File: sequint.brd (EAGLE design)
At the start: 70 x 80 mm, 72 parts, among them IC1 STM32F10XCXT6, Q1 MOSFET-NCHANNELSMD, Q2 MOSFET-NCHANNELSMD, Q3 MOSFET-NCHANNELSMD, Q4 MOSFET-NCHANNELSMD, Q5 16MHz, U1 LSM330DLCTRLGA, U2 MCP73831, U4 NRF24L01SMD

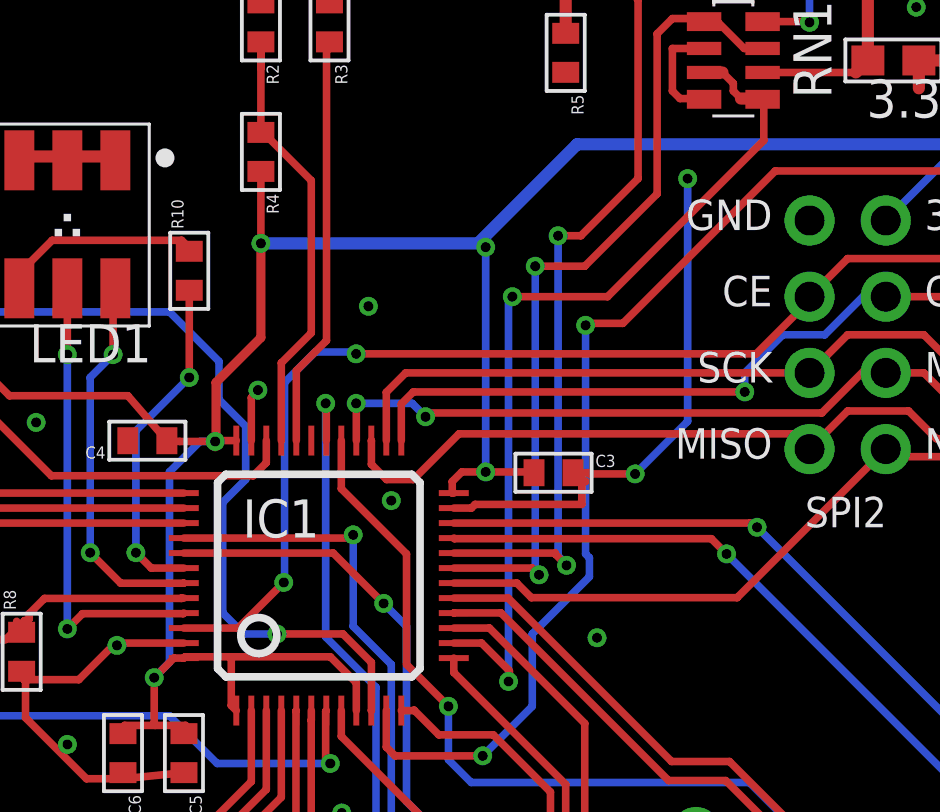
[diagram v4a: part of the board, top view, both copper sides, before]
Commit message: Move nrf-ce to pin 31 for better routing
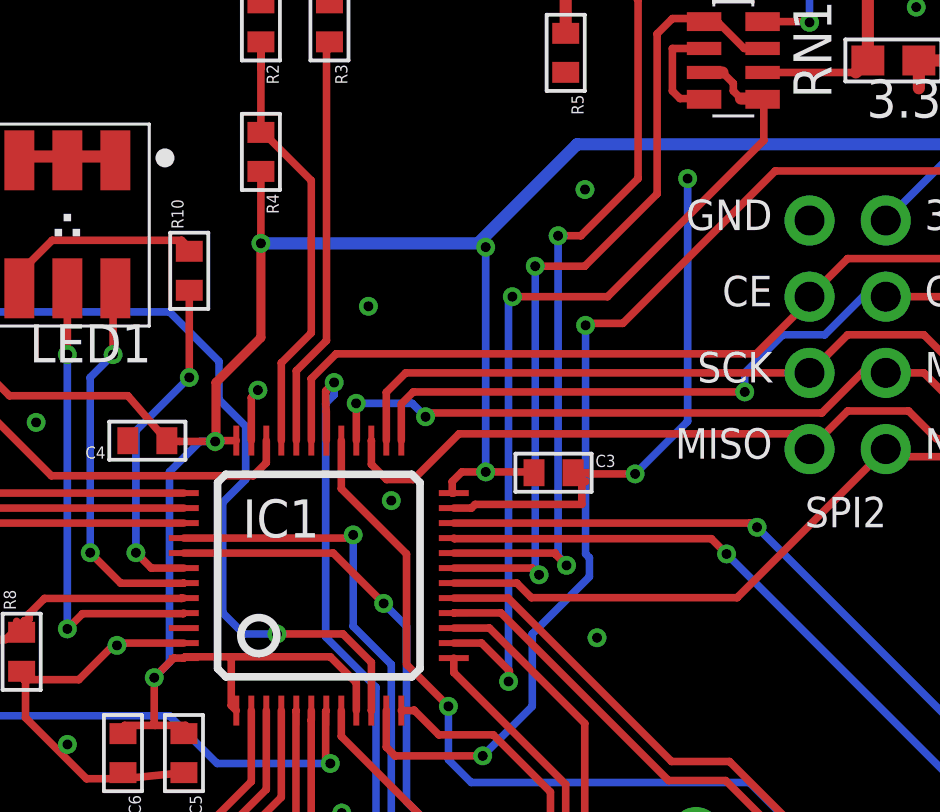
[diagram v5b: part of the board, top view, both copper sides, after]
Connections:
- net NRF-CE: now also IC1.31; no longer IC1.46
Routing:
- net NRF-CE: track 42.1 -> 32.5 mm, vias 2 -> 0
- net CS_G: track 57.1 -> 58.7 mm
- net GND: vias 29 -> 30
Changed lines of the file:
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@@
 <layer number="42" name="bRestrict" color="1" fill="10" visible="yes" active="yes"/>
 <layer number="43" name="vRestrict" color="2" fill="10" visible="yes" active="yes"/>
-<layer number="44" name="Drills" color="7" fill="1" visible="yes" active="yes"/>
+<layer number="44" name="Drills" color="7" fill="1" visible="no" active="yes"/>
 <layer number="45" name="Holes" color="7" fill="1" visible="yes" active="yes"/>
 <layer number="46" name="Milling" color="3" fill="1" visible="yes" active="yes"/>
@@
 <contactref element="U1" pad="10"/>
 <contactref element="LSM330_BRK" pad="2"/>
-<via x="24.991" y="53.914" extent="1-16" drill="0.3302"/>
 <wire x1="30.198" y1="34.864" x2="30.198" y2="26.355" width="0.254" layer="16"/>
 <wire x1="30.198" y1="26.355" x2="37.338" y2="19.304" width="0.254" layer="16"/>
@@
 <wire x1="26.67" y1="44.45" x2="26.67" y2="38.392" width="0.254" layer="16"/>
 <wire x1="26.67" y1="38.392" x2="30.198" y2="34.864" width="0.254" layer="16"/>
+<wire x1="24.991" y1="53.914" x2="24.991" y2="54.328" width="0.254" layer="1"/>
+<wire x1="24.991" y1="54.328" x2="25.273" y2="54.61" width="0.254" layer="1"/>
+<via x="25.273" y="54.61" extent="1-16" drill="0.3302"/>
+<wire x1="25.273" y1="54.61" x2="25.273" y2="54.196" width="0.254" layer="16"/>
+<wire x1="25.273" y1="54.196" x2="24.991" y2="53.914" width="0.254" layer="16"/>
 </signal>
 <signal name="INT1_A">
@@
 <contactref element="JS3" pad="1"/>
 <contactref element="JS4" pad="1"/>
-<wire x1="54.042" y1="27.741" x2="54.042" y2="28.341" width="0" layer="19" extent="1-1"/>
+<via x="33.634" y="61.042" extent="1-16" drill="0.3302"/>
 </signal>
 <signal name="3.3V">
@@
 </signal>
 <signal name="NRF-CE">
-<contactref element="IC1" pad="46"/>
 <contactref element="U4" pad="1"/>
 <contactref element="JPRF-B" pad="2"/>
@@
 <wire x1="46.962" y1="58.74" x2="42.39" y2="58.74" width="0.254" layer="1"/>
 <wire x1="42.39" y1="58.74" x2="41.12" y2="57.47" width="0.254" layer="1"/>
-<wire x1="20.2624" y1="46.4236" x2="22.0726" y2="46.4236" width="0.254" layer="1"/>
-<via x="23.594" y="47.945" extent="1-16" drill="0.3302"/>
-<wire x1="23.594" y1="47.945" x2="23.594" y2="47.978" width="0.254" layer="16"/>
-<via x="26.007" y="55.565" extent="1-16" drill="0.3302"/>
-<wire x1="26.007" y1="55.565" x2="39.342" y2="55.565" width="0.254" layer="1"/>
+<wire x1="25.339" y1="55.565" x2="39.342" y2="55.565" width="0.254" layer="1"/>
 <wire x1="39.342" y1="55.565" x2="41.12" y2="57.343" width="0.254" layer="1"/>
-<wire x1="22.0726" y1="46.4236" x2="23.594" y2="47.945" width="0.254" layer="1"/>
 <wire x1="41.12" y1="57.343" x2="41.12" y2="57.47" width="0.254" layer="1"/>
-<wire x1="23.594" y1="47.978" x2="23.622" y2="48.006" width="0.254" layer="16"/>
-<wire x1="23.622" y1="48.006" x2="23.622" y2="54.61" width="0.254" layer="16"/>
-<wire x1="23.622" y1="54.61" x2="24.638" y2="55.626" width="0.254" layer="16"/>
-<wire x1="24.638" y1="55.626" x2="25.946" y2="55.626" width="0.254" layer="16"/>
-<wire x1="25.946" y1="55.626" x2="26.007" y2="55.565" width="0.254" layer="16"/>
+<contactref element="IC1" pad="31"/>
+<wire x1="24.5124" y1="52.6736" x2="24.5124" y2="54.7384" width="0.254" layer="1"/>
+<wire x1="25.339" y1="55.565" x2="24.5124" y2="54.7384" width="0.254" layer="1"/>
+<wire x1="24.5124" y1="54.7384" x2="24.511" y2="54.737" width="0.254" layer="1"/>
 </signal>
 <signal name="BOOT0">

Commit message: rearrange more pins
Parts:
- moved C20 9.21 mm to (50.5, 36.8), turned to 90 degrees
- moved C22 8.64 mm to (58.7, 28.4), turned to 0 degrees
- moved C21 8.01 mm to (58.7, 26.7), turned to 0 degrees
- moved C2 0.07 mm to (54.6, 36.8)
- moved R1 0.07 mm to (52.3, 36.8)
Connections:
- removed net PC13: IC1.2, JP1.3
- removed net PC14: IC1.3, JP1.2
- removed net PC15: IC1.4, JP1.1
- net 5V-SENSE: now also IC1.30; no longer IC1.19
- net CS_A: now also IC1.19; no longer IC1.29
- net CS_G: now also IC1.18; no longer IC1.30
- net INT1_A: now also IC1.3; no longer IC1.40
- net INT2_G: now also IC1.4; no longer IC1.41
- net LIPO-STAT: now also IC1.31; no longer IC1.20
- net NRF-CE: now also IC1.29; no longer IC1.31
- net NRF-IRQ: now also IC1.20; no longer IC1.18
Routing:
- net PC15: track 17.6 -> 0.00 mm
- net PC14: track 15.9 -> 0.00 mm
- net PC13: track 14.2 -> 0.00 mm
- net CS_A: track 77.1 -> 65.2 mm, vias 3 -> 2
- net GND: track 124.1 -> 113.0 mm, vias 30 -> 39
- net INT1_A: track 45.6 -> 38.2 mm
- net 3.3V: track 214.8 -> 222.1 mm, vias 14 -> 13
- net INT2_G: track 45.9 -> 39.1 mm
- net INT1_G: track 21.7 -> 24.7 mm
- net 5V-SENSE: track 28.0 -> 25.0 mm, vias 2 -> 0
- net LIPO-STAT: track 27.2 -> 24.5 mm, vias 2 -> 0
- net CS_G: track 58.7 -> 61.3 mm, vias 1 -> 2
- net TMR2-CH1: track 53.1 -> 50.6 mm
- net NRF-CE: track 32.5 -> 31.5 mm
- net NRST: track 20.8 -> 21.5 mm

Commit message: Move LED
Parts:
- moved R10 27.6 mm to (5.08, 35.4), turned to 270 degrees
- moved LED1 27.4 mm to (9.02, 33.5), turned to 0 degrees
- moved JP1 27.2 mm to (14.6, 64.2)
- moved BOOT 4.92 mm to (15.3, 43.4), turned to 270 degrees
- moved R8 1.99 mm to (13.0, 45.0), turned to 270 degrees
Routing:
- net GND: track 113.0 -> 96.2 mm, vias 39 -> 40
- net RGB-R: track 11.3 -> 22.8 mm, vias 2 -> 0
- net RGB-B: track 12.9 -> 21.5 mm, vias 2 -> 0
- net 3.3V: track 222.1 -> 215.2 mm, vias 13 -> 12
- net RGB-G: track 15.5 -> 18.4 mm, vias 2 -> 0
- net RGB-RP: track 6.93 -> 8.18 mm
- net BOOT0: track 9.67 -> 8.56 mm
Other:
- board text removed: "PC13"
- board text removed: "PC14"
- board text removed: "PC15"

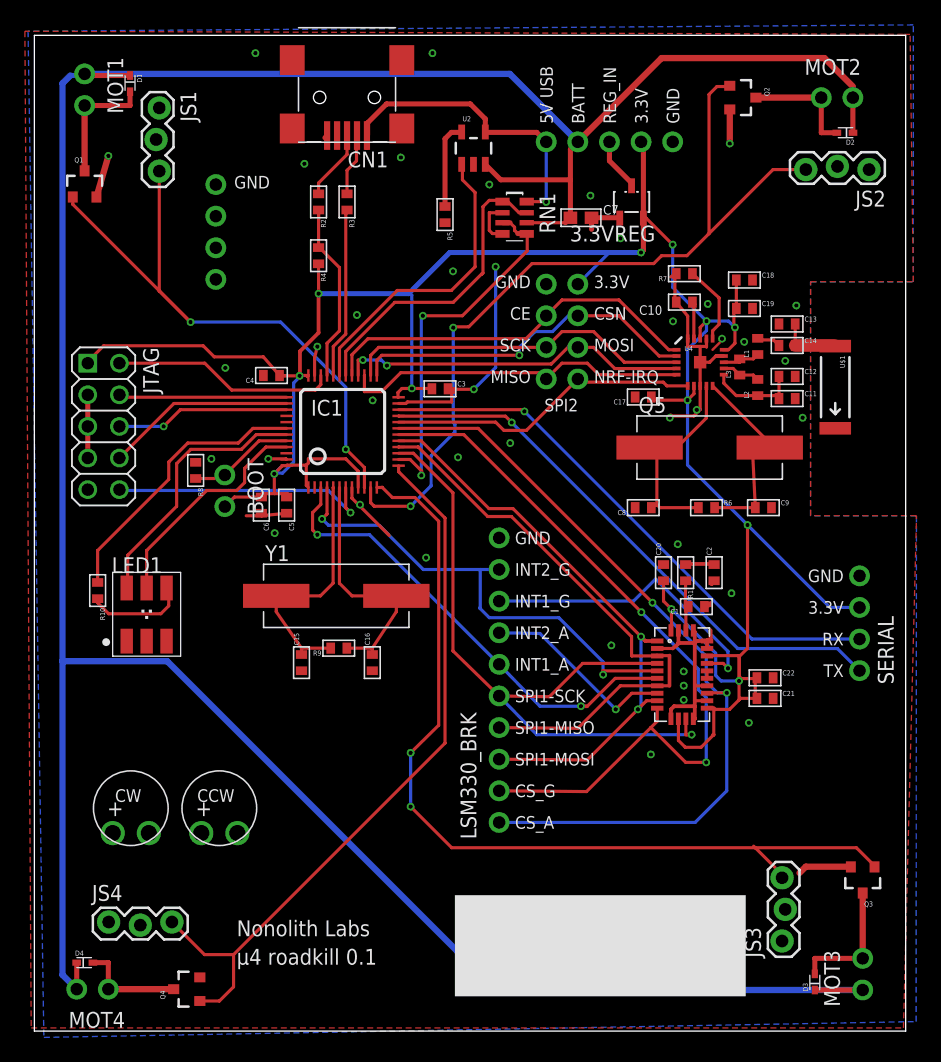
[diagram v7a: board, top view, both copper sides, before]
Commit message: Move USART to USART1, which supports bootloader.
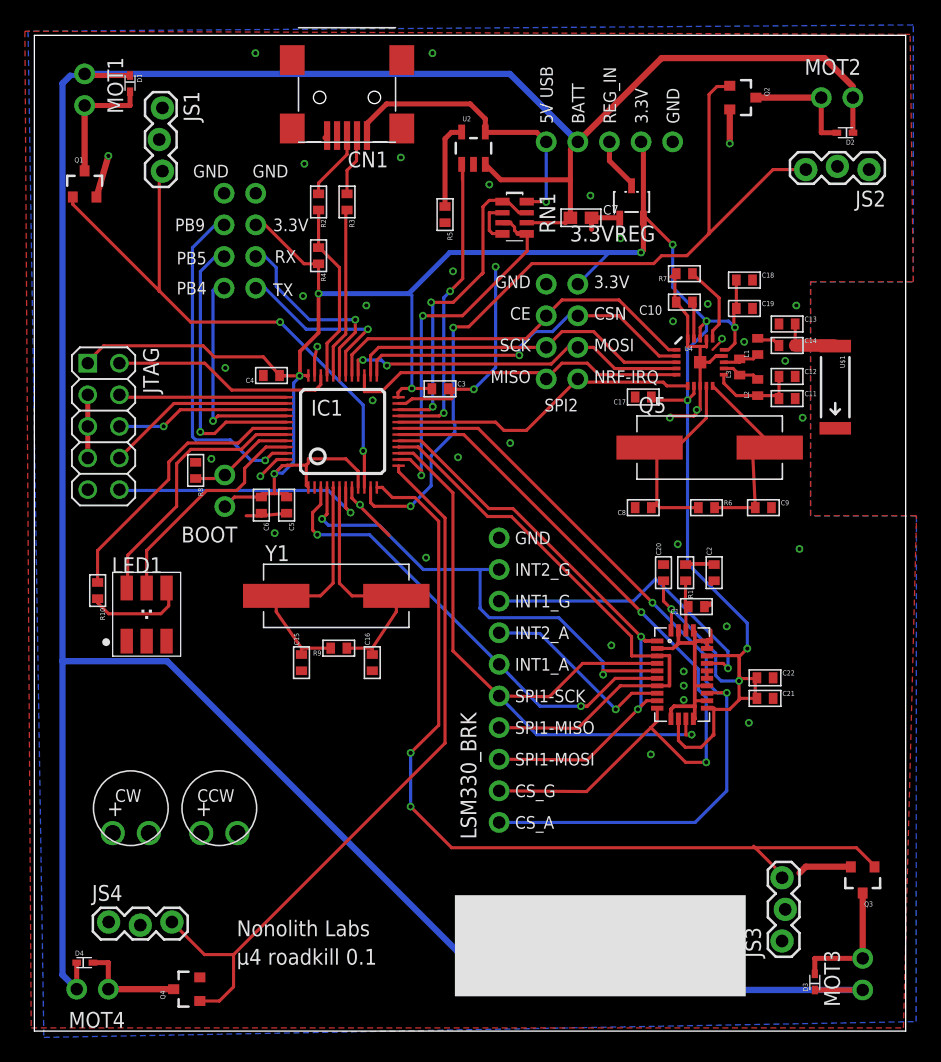
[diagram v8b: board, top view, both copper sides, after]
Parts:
- moved SERIAL 57.4 mm to (17.8, 63.5)
- moved JP1 0.96 mm to (15.2, 63.5)
- moved JS1 0.25 mm to (10.2, 74.2)
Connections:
- new net PB4: IC1.40, JP1.1
- new net PB5: IC1.41, JP1.2
- new net PB9: IC1.46, JP1.3
- net 5V-SENSE: now also IC1.22; no longer IC1.30
- net LIPO-STAT: now also IC1.21; no longer IC1.31
- net RX: now also IC1.31; no longer IC1.22
- net TX: now also IC1.30; no longer IC1.21
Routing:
- net TX: track 45.6 -> 14.8 mm
- net RX: track 44.6 -> 16.0 mm
- net PB9: track 0.00 -> 27.1 mm, vias 0 -> 1
- net PB5: track 0.00 -> 22.7 mm, vias 0 -> 1
- net PB4: track 0.00 -> 17.5 mm, vias 0 -> 1
- net 3.3V: track 215.2 -> 209.9 mm
- net TMR2-CH1: track 50.6 -> 47.1 mm
- net LIPO-STAT: track 24.5 -> 25.5 mm, vias 0 -> 2
- net GND: track 96.2 -> 97.2 mm, vias 40 -> 42
- net 5V-SENSE: track 25.0 -> 25.9 mm, vias 0 -> 2
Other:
- board text added: "PB4"
- board text added: "PB5"
- board text added: "PB9"
